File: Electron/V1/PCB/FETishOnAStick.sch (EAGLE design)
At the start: 18 parts, among them Q1 FDD8780 or FDD8451, Q2 BSS138 - 200mA/50V, Q3 FDD8780 or FDD8451

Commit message: Initial version.
NB: Missing track for A4.
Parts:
- R1, R7, R8: value 0R -> 10R
- R2, R6, R9: value 0R -> 10k
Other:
- note added: "Electron: PWM is available on D0, D1, D2, D3, B0, B1, B2, B3, A4, A5, WKP, RX, TX"
- note added: "PWM may be used on A4 while D3 is used as a GPIO"
- note added: "Photon & Electron: PWM timer peripheral is duplicated on two pins (A5/D2) and (A4/D3) for 7 total independent PWM outputs"
- note added: "Photon: PWM is available on D0, D1, D2, D3, A4, A5, WKP, RX, TX"
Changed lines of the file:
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@@
 <part name="Q1" library="SparkFun-DiscreteSemi" deviceset="MOSFET-NCHANNEL" device="FDD8780" value="FDD8780 or FDD8451"/>
 <part name="Q2" library="SparkFun-DiscreteSemi" deviceset="MOSFET-NCHANNEL" device="BSS138" value="BSS138 - 200mA/50V"/>
-<part name="R6" library="SparkFun-Resistors" deviceset="RESISTOR" device="0805-RES" value="0R"/>
-<part name="R7" library="SparkFun-Resistors" deviceset="RESISTOR" device="0805-RES" value="0R"/>
-<part name="R8" library="SparkFun-Resistors" deviceset="RESISTOR" device="0805-RES" value="0R"/>
-<part name="R9" library="SparkFun-Resistors" deviceset="RESISTOR" device="0805-RES" value="0R"/>
+<part name="R6" library="SparkFun-Resistors" deviceset="RESISTOR" device="0805-RES" value="10k"/>
+<part name="R7" library="SparkFun-Resistors" deviceset="RESISTOR" device="0805-RES" value="10R"/>
+<part name="R8" library="SparkFun-Resistors" deviceset="RESISTOR" device="0805-RES" value="10R"/>
+<part name="R9" library="SparkFun-Resistors" deviceset="RESISTOR" device="0805-RES" value="10k"/>
 <part name="GND12" library="SparkFun-Aesthetics" deviceset="DGND" device=""/>
 <part name="GND13" library="SparkFun-Aesthetics" deviceset="DGND" device=""/>
 <part name="Q3" library="SparkFun-DiscreteSemi" deviceset="MOSFET-NCHANNEL" device="FDD8780" value="FDD8780 or FDD8451"/>
-<part name="R1" library="SparkFun-Resistors" deviceset="RESISTOR" device="0805-RES" value="0R"/>
-<part name="R2" library="SparkFun-Resistors" deviceset="RESISTOR" device="0805-RES" value="0R"/>
+<part name="R1" library="SparkFun-Resistors" deviceset="RESISTOR" device="0805-RES" value="10R"/>
+<part name="R2" library="SparkFun-Resistors" deviceset="RESISTOR" device="0805-RES" value="10k"/>
 <part name="GND6" library="SparkFun-Aesthetics" deviceset="DGND" device=""/>
 <part name="GND7" library="SparkFun-Aesthetics" deviceset="DGND" device=""/>
@@
 <text x="58.42" y="48.26" size="1.778" layer="97">High Current</text>
 <text x="22.86" y="137.16" size="1.778" layer="97">Low Current (200mA max)</text>
+<text x="129.54" y="86.36" size="1.778" layer="97">Photon: PWM is available on D0, D1, D2, D3, A4, A5, WKP, RX, TX</text>
+<text x="129.54" y="78.74" size="1.778" layer="97">Photon &amp; Electron: PWM timer peripheral is duplicated on two pins (A5/D2) and (A4/D3) for 7 total independent PWM outputs</text>
+<text x="129.54" y="83.82" size="1.778" layer="97">Electron: PWM is available on D0, D1, D2, D3, B0, B1, B2, B3, A4, A5, WKP, RX, TX</text>
+<text x="129.54" y="76.2" size="1.778" layer="97">PWM may be used on A4 while D3 is used as a GPIO</text>
 </plain>
 <instances>

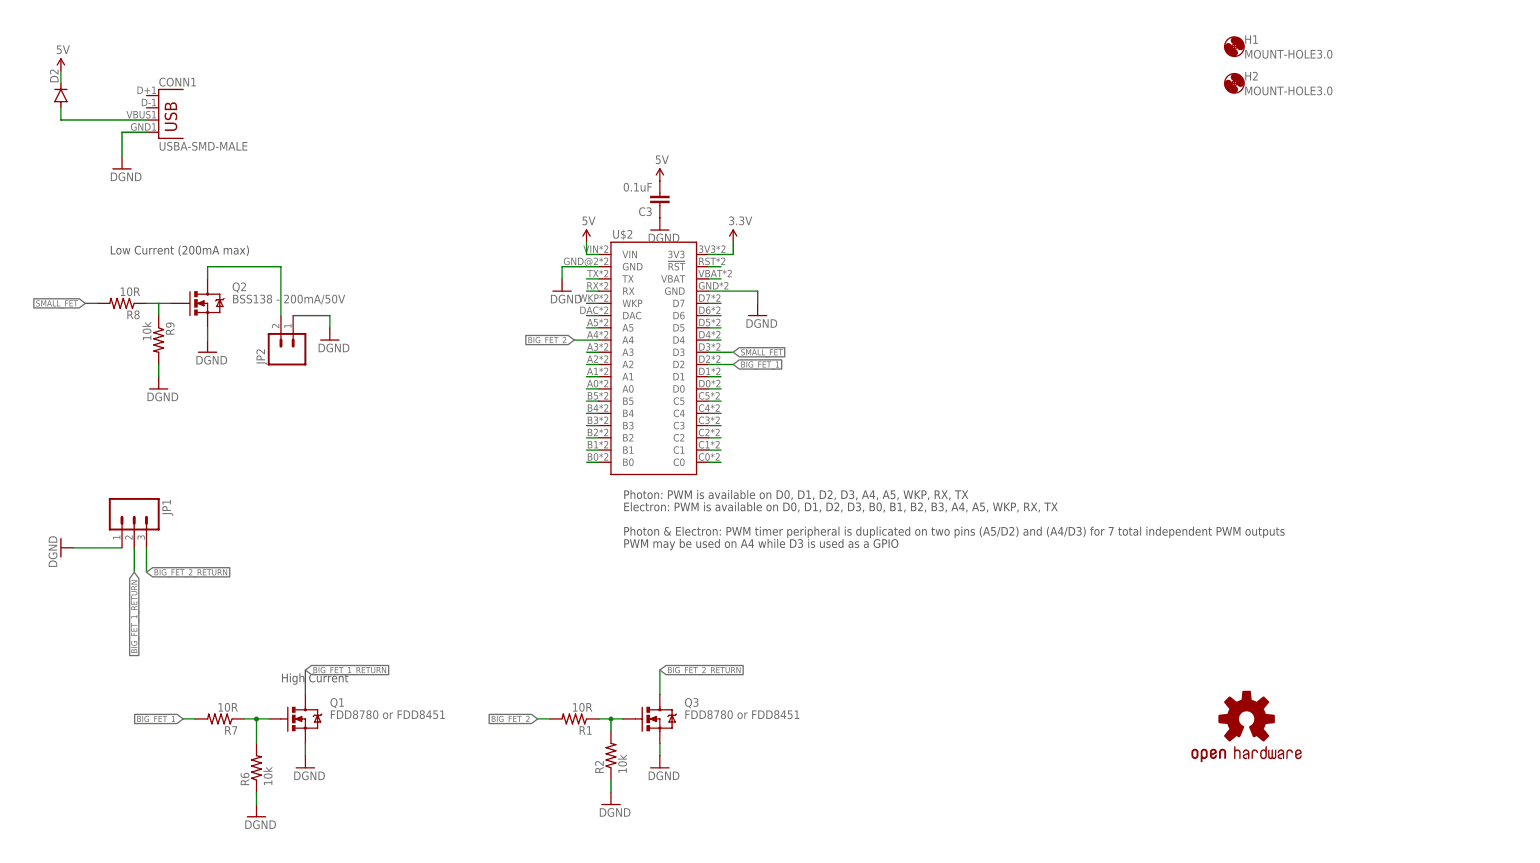
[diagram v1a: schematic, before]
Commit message: Updated identifiers, tidied up and added BOMs and images
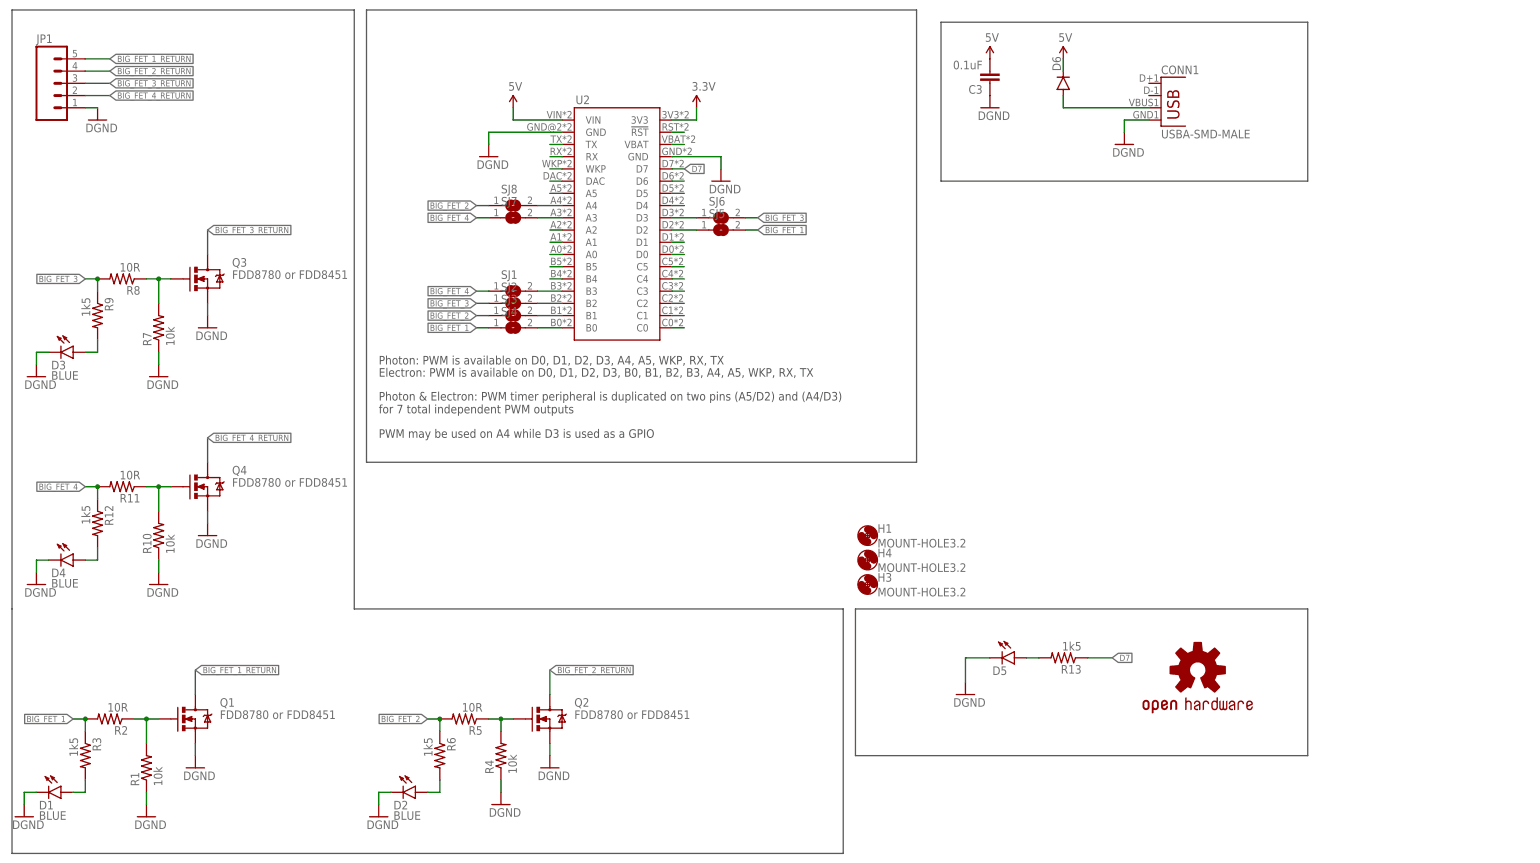
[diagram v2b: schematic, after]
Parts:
- removed H2: MOUNT-HOLE3.0, holes:MOUNT-HOLE3.0
- removed JP2: (no value), SparkFun-Connectors:M02POLAR
- removed LOGO2: OSHW-LOGOS, SparkFun-Aesthetics:OSHW-LOGOS
- removed U$2: ELECTRONDUALNAMED, Tinamous:ELECTRONDUALNAMED
- added D1, D3, D4: BLUE, SparkFun-LED:LED-BLUE1206
- added D5: (no value), SparkFun-LED:LED1206-BOTTOM
- added D6: (no value), SparkFun-DiscreteSemi:DIODESMA
- added H3, H4: MOUNT-HOLE3.2, holes:MOUNT-HOLE3.2
- added LOGO1: OSHW-LOGOM, SparkFun-Aesthetics:OSHW-LOGOM
- added Q4: FDD8780 or FDD8451, SparkFun-DiscreteSemi:MOSFET-NCHANNELFDD8780
- added R10, R4: 10k, SparkFun-Resistors:RESISTOR0805-RES
- added R11, R5: 10R, SparkFun-Resistors:RESISTOR0805-RES
- added R12, R13, R3: 1k5, SparkFun-Resistors:RESISTOR0805-RES
- added SJ1, SJ2, SJ3, SJ4, SJ5, SJ6, SJ7, SJ8: (no value), jumper:SJ
- added U2: ELECTRONDUALNAMED, Tinamous:ELECTRONDUALNAMED
- D2: value (none) -> BLUE; device SparkFun-DiscreteSemi:DIODESMA -> SparkFun-LED:LED-BLUE1206
- H1: value MOUNT-HOLE3.0 -> MOUNT-HOLE3.2; device holes:MOUNT-HOLE3.0 -> holes:MOUNT-HOLE3.2
- JP1: device SparkFun-Connectors:M03-SCREW-5MM -> SparkFun-Connectors:M05SCREW
- Q2: value BSS138 - 200mA/50V -> FDD8780 or FDD8451; device SparkFun-DiscreteSemi:MOSFET-NCHANNELBSS138 -> SparkFun-DiscreteSemi:MOSFET-NCHANNELFDD8780
- R1, R7: value 10R -> 10k
- R2: value 10k -> 10R
- R6, R9: value 10k -> 1k5
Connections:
- removed net N$3: Q3.G, R1.1, R2.2
- removed net SMALL_FET: R8.2, U$2.D3
- removed net SMALL_FET_RETURN: JP2.2, Q2.D
- new net BIG_FET_3: R8.2, R9.1, SJ2.1, SJ6.2
- new net BIG_FET_3_RETURN: JP1.3, Q3.D
- new net BIG_FET_4: R11.2, R12.1, SJ1.1, SJ7.1
- new net BIG_FET_4_RETURN: JP1.2, Q4.D
- new net D7: R13.1, U2.D7
- new net N$105: Q2.G, R4.2, R5.1
- new net N$12: D2.A, R6.2
- new net N$19: D5.A, R13.2
- new net N$21: Q3.G, R7.2, R8.1
- new net N$22: D3.A, R9.2
- new net N$30: SJ8.2, U2.A4
- new net N$4: Q4.G, R10.2, R11.1
- new net N$43: SJ6.1, U2.D3
- new net N$49: SJ5.1, U2.D2
- net 3.3V: now also U2.3V3; no longer U$2.3V3
- net 5V: now also D6.C, U2.VIN; no longer D2.C, U$2.VIN
- net BIG_FET_1: now also R2.2, R3.1, SJ4.1, SJ5.2; no longer R7.2, U$2.D2
- net BIG_FET_1_RETURN: now also JP1.5; no longer JP1.2
- net BIG_FET_2: now also R5.2, R6.1, SJ3.1, SJ8.1; no longer R1.2, U$2.A4
- net BIG_FET_2_RETURN: now also JP1.4, Q2.D; no longer JP1.3, Q3.D
- net GND: now also D1.C, D2.C, D3.C, D4.C, D5.C, Q4.S, R1.1, R10.1, R4.1, R7.1, U2.GND, U2.GND@2; no longer JP2.1, R2.1, R6.1, R9.2, U$2.GND, U$2.GND@2
- net N$1: now also D6.A; no longer D2.A
- net N$11: now also D1.A, R3.2; no longer U$2.D7
- net N$13: now also D4.A, R12.2; no longer Q2.G, R8.1, R9.1
- net N$15: now also U2.D6; no longer U$2.D6
- net N$16: now also U2.D5; no longer U$2.D5
- net N$20: now also U2.D4; no longer U$2.D4
- net N$23: now also U2.C5; no longer U$2.C5
- net N$24: now also U2.C4; no longer U$2.C4
- net N$25: now also U2.C3; no longer U$2.C3
- net N$26: now also U2.C2; no longer U$2.C2
- net N$27: now also R1.2, R2.1; no longer R6.2, R7.1
- net N$28: now also U2.C1; no longer U$2.C1
- net N$29: now also U2.C0; no longer U$2.C0
- net N$31: now also SJ4.2, U2.B0; no longer U$2.B0
- net N$33: now also SJ3.2, U2.B1; no longer U$2.B1
- net N$35: now also SJ2.2, U2.B2; no longer U$2.B2
- net N$36: now also SJ1.2, U2.B3; no longer U$2.B3
- net N$37: now also U2.B4; no longer U$2.B4
- net N$38: now also U2.B5; no longer U$2.B5
- net N$39: now also U2.A0; no longer U$2.A0
- net N$40: now also U2.A1; no longer U$2.A1
- net N$41: now also U2.A2; no longer U$2.A2
- net N$42: now also SJ7.2, U2.A3; no longer U$2.A3
- net N$44: now also U2.A5; no longer U$2.A5
- net N$45: now also U2.DAC; no longer U$2.DAC
- net N$46: now also U2.WKP; no longer U$2.WKP
- net N$47: now also U2.RX; no longer U$2.RX
- net N$48: now also U2.TX; no longer U$2.TX
- net N$6: now also U2.VBAT; no longer U$2.VBAT
- net N$7: now also U2.!RST; no longer U$2.!RST
- net SCL: now also U2.D1; no longer U$2.D1
- net SDA: now also U2.D0; no longer U$2.D0
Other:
- note removed: "High Current"
- note removed: "Low Current (200mA max)"
- moved on the sheet: C3, CONN1, H1, Q1, Q2, Q3, R1, R2, R6, R7, R8, R9
